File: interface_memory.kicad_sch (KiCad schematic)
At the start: 52 parts, among them IC304 15 A4, IC509 M41464, IC510 M41464, IC512 LC3517BML, IC513 D43100AGW, IC514 D43100AGW, IC515 D23HC4001EGW, IC516 74LS244, IC517 74LS244, IC518 74LS244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

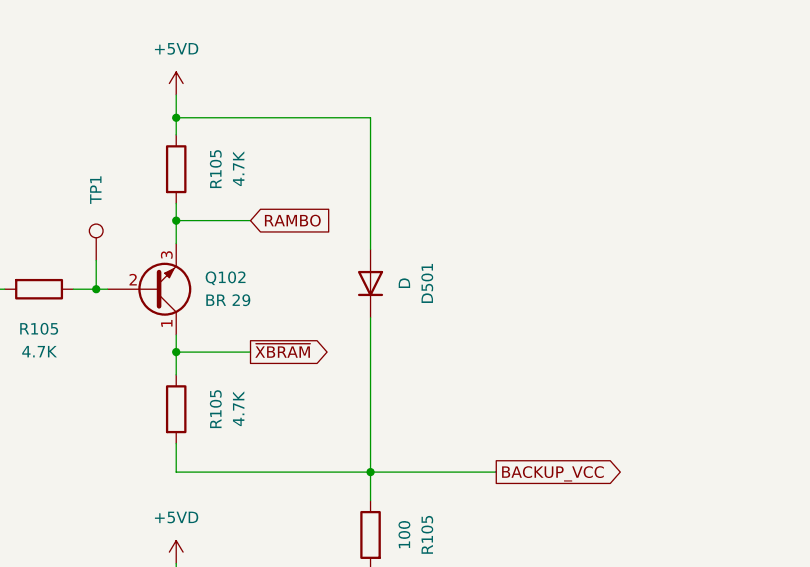
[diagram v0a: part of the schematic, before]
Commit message: Add markings for SMD Ds and Qs.
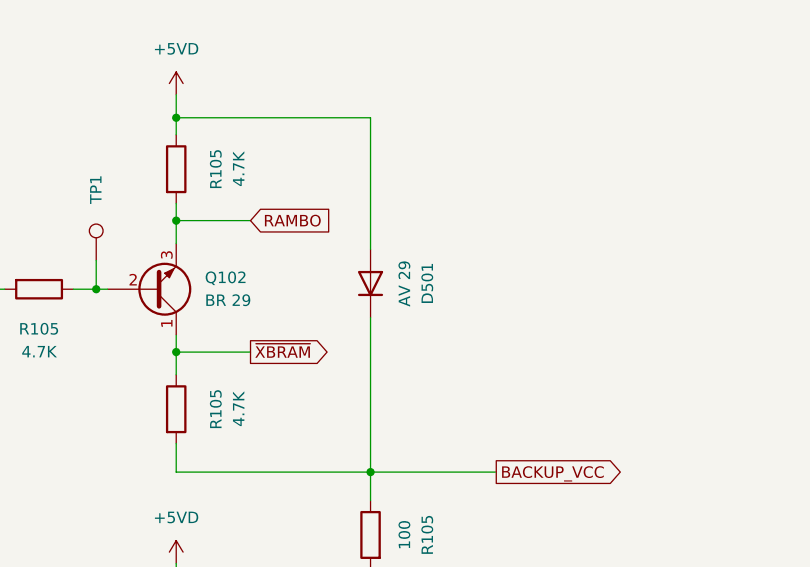
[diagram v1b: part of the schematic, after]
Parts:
- D501: value D -> AV 29
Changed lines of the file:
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@@
       (effects (font (size 1.27 1.27)))
     )
-    (property "Value" "D" (at 264.16 216.535 0)
+    (property "Value" "AV 29" (at 264.16 216.535 0)
       (effects (font (size 1.27 1.27)))
     )

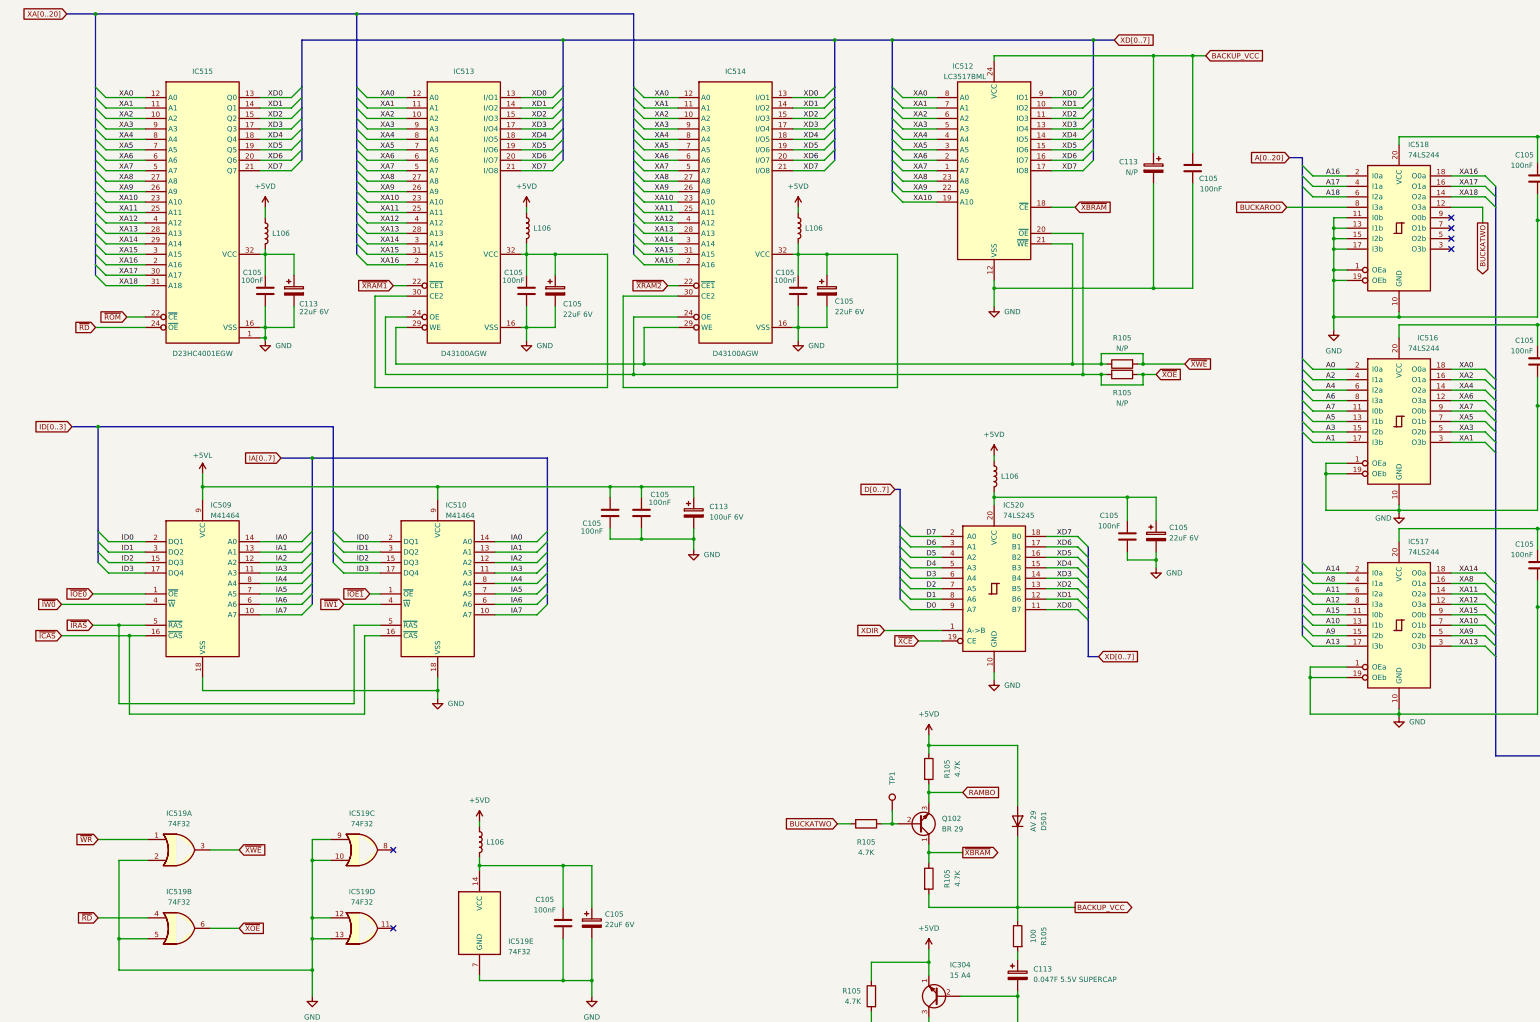
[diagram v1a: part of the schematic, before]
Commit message: More schematic clean-up/annotation.
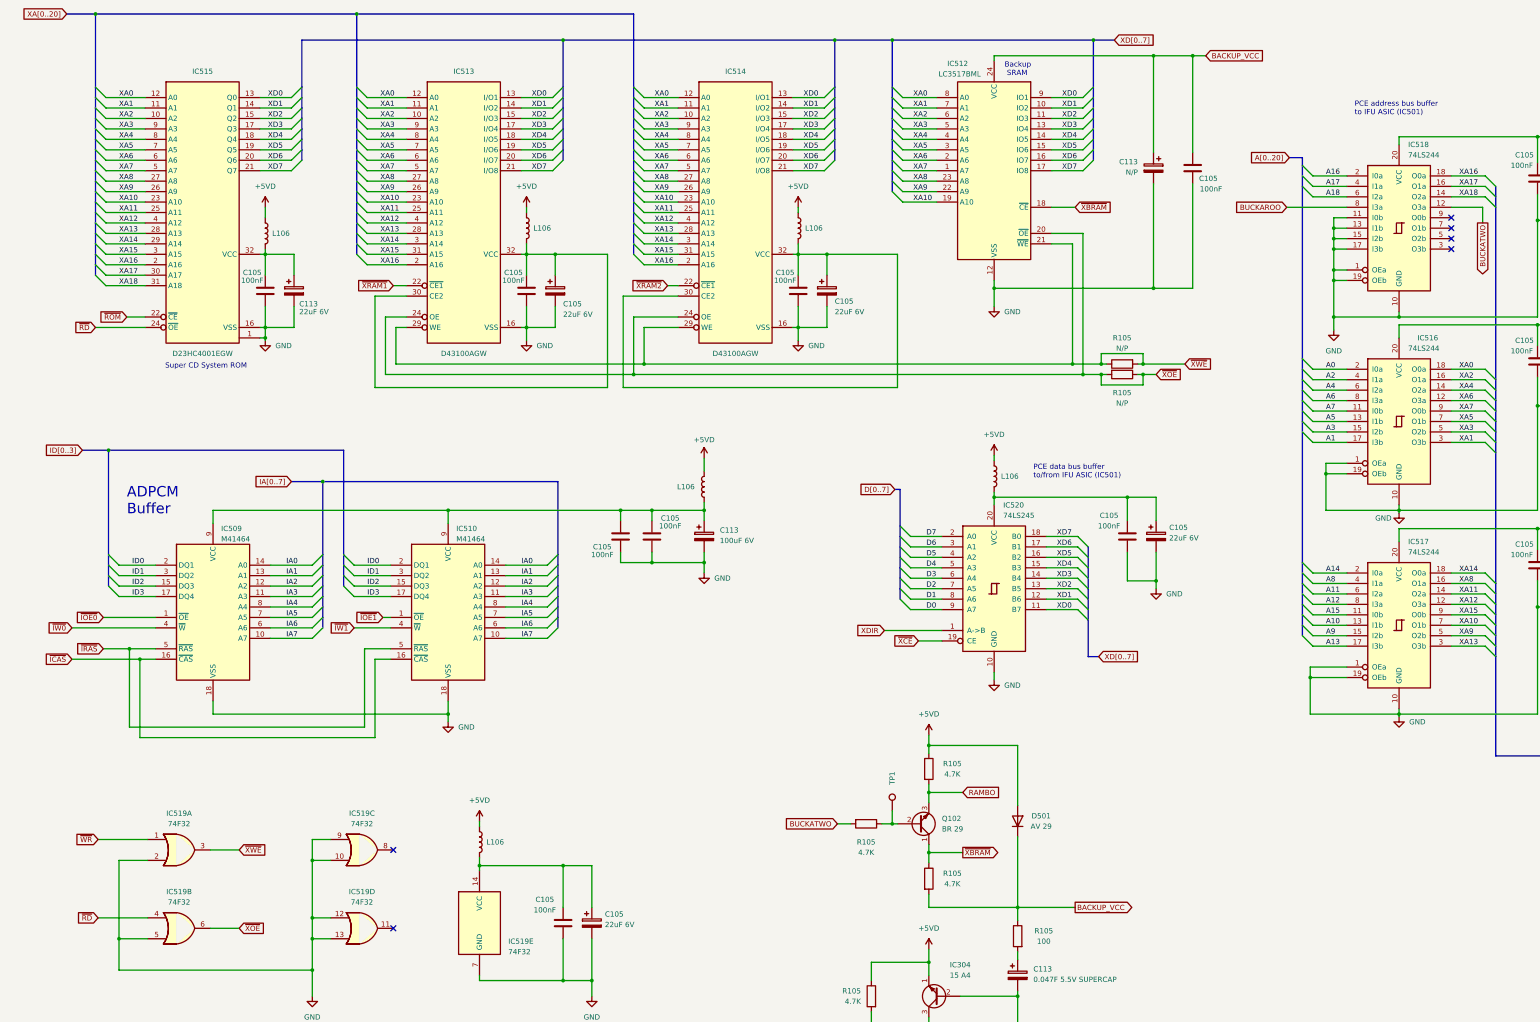
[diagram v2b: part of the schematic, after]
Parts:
- added L106: ~, A-PCENGINE:SMD_0805_Narrow_Long, symbol Device:L
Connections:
- net +5VD: now also L106.2
- net +5VL: no longer names the net of C105.2, C105.2, C113.1, IC509.9 (VCC), IC510.9 (VCC)
- net +5VL: now also L106.1
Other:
- note added: "ADPCM Buffer"
- note added: "Backup SRAM"
- note added: "PCE address bus buffer to IFU ASIC (IC501)"
- note added: "PCE data bus buffer to/from IFU ASIC (IC501)"
- note added: "Super CD System ROM"
- company: (none) -> By Cosam
- title: (none) -> PC Engine Duo IFU Memory
- moved on the sheet: C105, C113, IC509, IC510

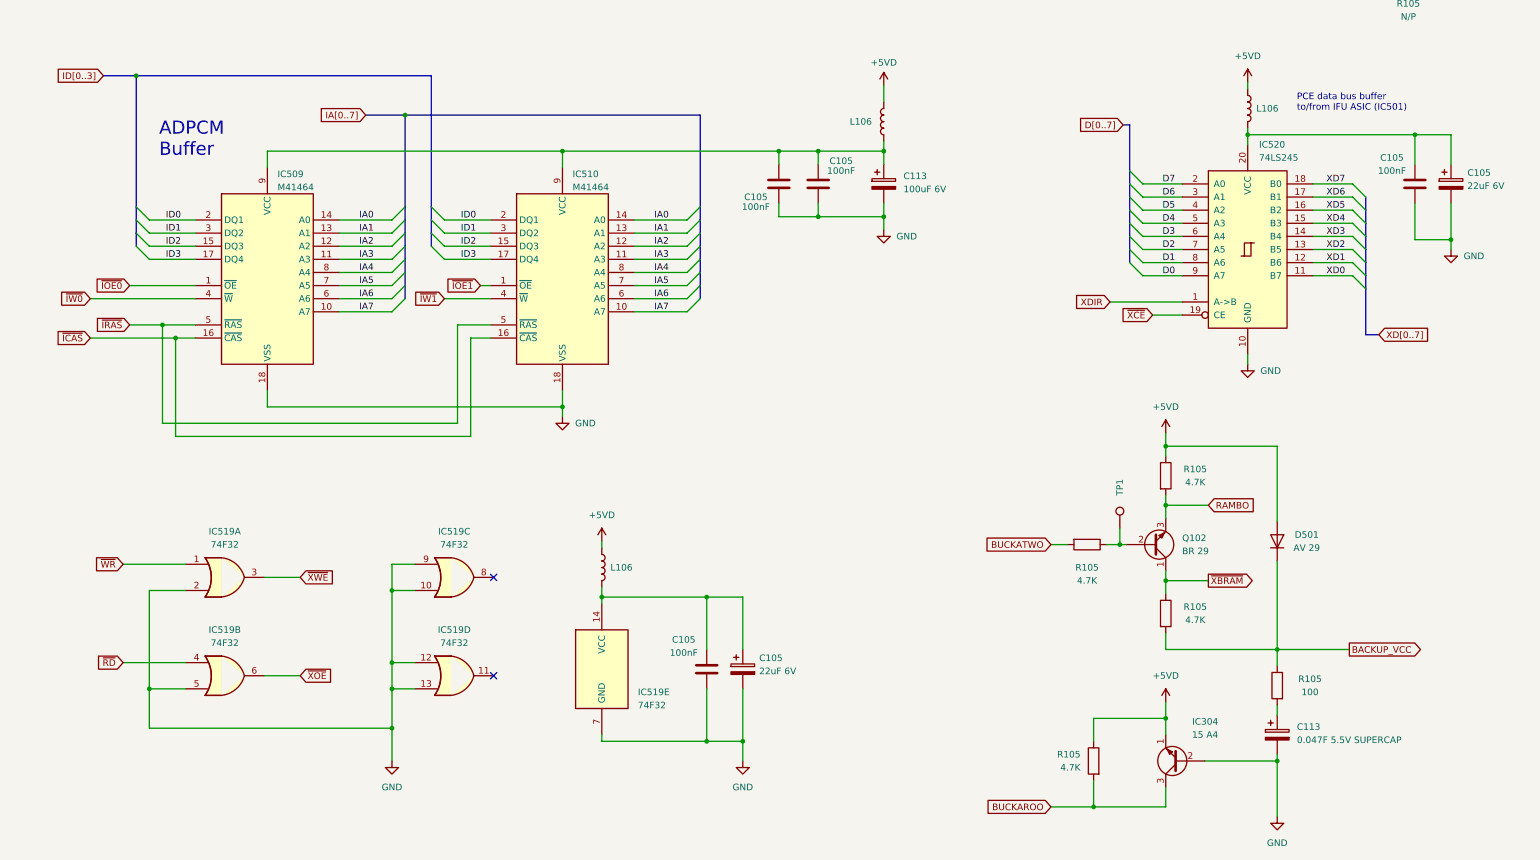
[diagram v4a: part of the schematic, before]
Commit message: Minor schematic/silkscreen changes.
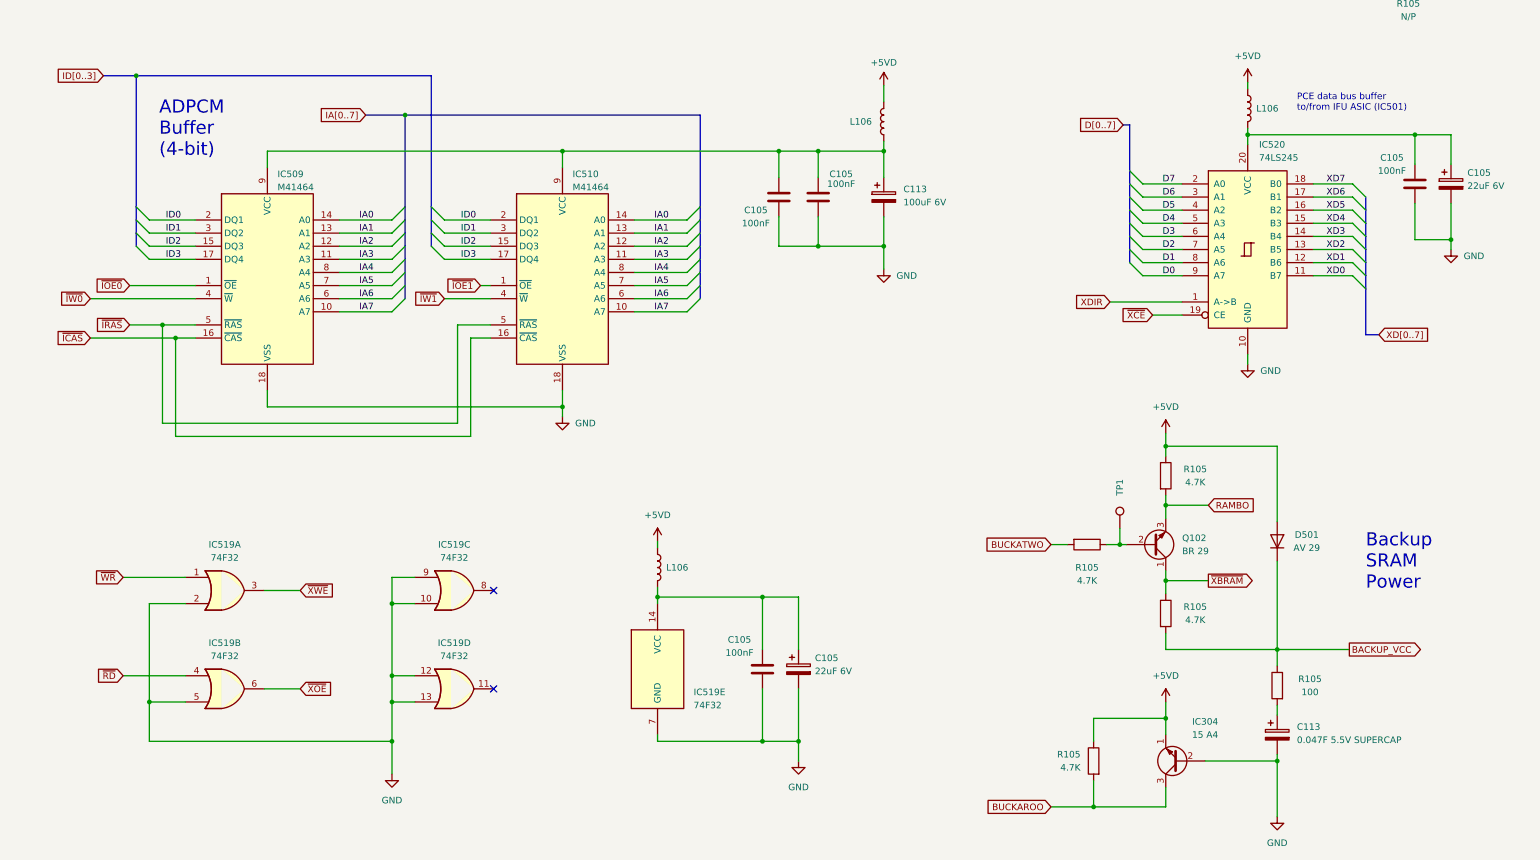
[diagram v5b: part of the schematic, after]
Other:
- note added: "ADPCM Buffer (4-bit)"
- note added: "Backup SRAM Power"
- note removed: "ADPCM Buffer"
- moved on the sheet: C105, C113, IC519A, IC519B, IC519C, IC519D, IC519E, L106
